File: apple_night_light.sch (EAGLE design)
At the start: 39 parts, among them U2 INA219AIDCNR, U3 ATSHA204-TSU, Y1 16MHZ

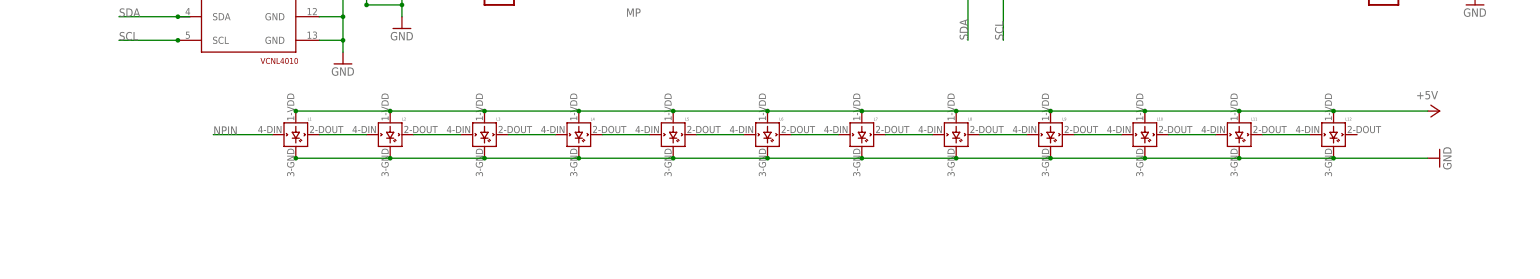
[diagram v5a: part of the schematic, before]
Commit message: converting to dotstar LEDs, still some hookup work needed
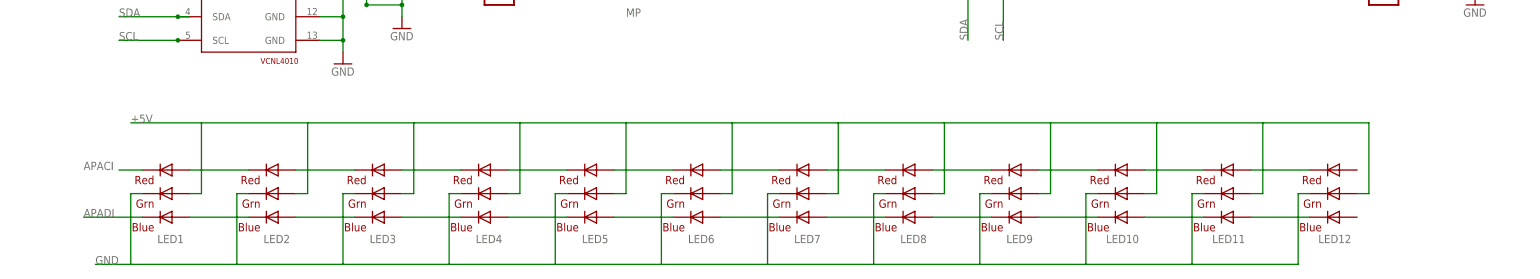
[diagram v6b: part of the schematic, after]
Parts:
- removed L1, L10, L11, L12, L2, L3, L4, L5, L6, L7, L8, L9: WS2812B, adafruit:WS2812B
- added LED1, LED10, LED11, LED12, LED2, LED3, LED4, LED5, LED6, LED7, LED8, LED9: RGBLED5050, adafruit:RGBLED5050
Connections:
- removed net N$14: L5.DOUT, L6.DIN
- removed net N$20: L7.DOUT, L8.DIN
- removed net N$28: L4.DOUT, L5.DIN
- new net APACI: LED1.RED_C
- new net APACI1: LED3.RED_A, LED4.RED_C
- new net APACI2: LED6.RED_A, LED7.RED_C
- new net APACI3: LED10.RED_C, LED9.RED_A
- new net APADI: LED1.BLUE_C
- new net N$1: LED1.RED_A, LED2.RED_C
- new net N$15: LED4.RED_A, LED5.RED_C
- new net N$18: LED4.BLUE_A, LED5.BLUE_C
- new net N$26: LED8.BLUE_A, LED9.BLUE_C
- new net N$30: LED10.RED_A, LED11.RED_C
- new net N$31: LED11.RED_A, LED12.RED_C
- new net N$32: LED10.BLUE_A, LED11.BLUE_C
- new net N$35: LED11.BLUE_A, LED12.BLUE_C
- new net N$5: LED2.BLUE_A, LED3.BLUE_C
- new net N$6: LED3.BLUE_A, LED4.BLUE_C
- new net N$8: LED6.BLUE_A, LED7.BLUE_C
- net +5V: now also LED1.GREEN_A, LED10.GREEN_A, LED11.GREEN_A, LED12.GREEN_A, LED2.GREEN_A, LED3.GREEN_A, LED4.GREEN_A, LED5.GREEN_A, LED6.GREEN_A, LED7.GREEN_A, LED8.GREEN_A, LED9.GREEN_A; no longer L1.VDD, L10.VDD, L11.VDD, L12.VDD, L2.VDD, L3.VDD, L4.VDD, L5.VDD, L6.VDD, L7.VDD, L8.VDD, L9.VDD
- net GND: now also LED1.GREEN_C, LED10.GREEN_C, LED11.GREEN_C, LED12.GREEN_C, LED2.GREEN_C, LED3.GREEN_C, LED4.GREEN_C, LED5.GREEN_C, LED6.GREEN_C, LED7.GREEN_C, LED8.GREEN_C, LED9.GREEN_C; no longer L1.GND, L10.GND, L11.GND, L12.GND, L2.GND, L3.GND, L4.GND, L5.GND, L6.GND, L7.GND, L8.GND, L9.GND
- net N$12: now also LED10.BLUE_C, LED9.BLUE_A; no longer L6.DOUT, L7.DIN
- net N$17: now also LED5.RED_A, LED6.RED_C; no longer L10.DIN, L9.DOUT
- net N$19: now also LED5.BLUE_A, LED6.BLUE_C; no longer L8.DOUT, L9.DIN
- net N$2: now also LED2.RED_A, LED3.RED_C; no longer L2.DOUT, L3.DIN
- net N$23: now also LED7.RED_A, LED8.RED_C; no longer L3.DOUT, L4.DIN
- net N$24: now also LED8.RED_A, LED9.RED_C; no longer L11.DOUT, L12.DIN
- net N$25: now also LED7.BLUE_A, LED8.BLUE_C; no longer L10.DOUT, L11.DIN
- net N$3: now also LED1.BLUE_A, LED2.BLUE_C; no longer L1.DOUT, L2.DIN
- net NPIN: no longer L1.DIN

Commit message: re-laying out the board and separating panels to an extent
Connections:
- removed net APACI: LED1.RED_C
- removed net APADI: LED1.BLUE_C
- net MOSI: now also LED1.BLUE_C
- net SCK: now also LED1.RED_C
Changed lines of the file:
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@@
 <label x="121.92" y="63.5" size="1.778" layer="95" xref="yes"/>
+</segment>
+<segment>
+<pinref part="LED1" gate="G$1" pin="BLUE_C"/>
+<wire x1="-119.38" y1="-25.4" x2="-132.08" y2="-25.4" width="0.1524" layer="91"/>
+<label x="-132.08" y="-25.4" size="1.778" layer="95"/>
 </segment>
 </net>
@@
 <wire x1="96.52" y1="63.5" x2="88.9" y2="63.5" width="0.1524" layer="91"/>
 <label x="88.9" y="63.5" size="1.778" layer="95" rot="MR0" xref="yes"/>
+</segment>
+<segment>
+<pinref part="LED1" gate="G$1" pin="RED_C"/>
+<wire x1="-119.38" y1="-15.24" x2="-124.46" y2="-15.24" width="0.1524" layer="91"/>
+<label x="-132.08" y="-15.24" size="1.778" layer="95"/>
 </segment>
 </net>
@@
 </segment>
 </net>
-<net name="APADI" class="0">
-<segment>
-<pinref part="LED1" gate="G$1" pin="BLUE_C"/>
-<wire x1="-119.38" y1="-25.4" x2="-132.08" y2="-25.4" width="0.1524" layer="91"/>
-<label x="-132.08" y="-25.4" size="1.778" layer="95"/>
-</segment>
-</net>
-<net name="APACI" class="0">
-<segment>
-<pinref part="LED1" gate="G$1" pin="RED_C"/>
-<wire x1="-119.38" y1="-15.24" x2="-124.46" y2="-15.24" width="0.1524" layer="91"/>
-<label x="-132.08" y="-15.24" size="1.778" layer="95"/>
-</segment>
-</net>

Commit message: adding balance board for space usage, tightening things up
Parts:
- added A0, A1: TPB1,27, testpad:TPB1,27
- added JP3: (no value), SparkFun-Connectors:M06NO_SILK_FEMALE_PTH
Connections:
- new net N$43: A0.TP, U2.A0
- new net N$44: A1.TP, U2.A1
- new net N$46: AOUT.1, C1.2, C2.-, C3.-, C4.2, C5.2, C7.2, DOUT.1, JP1.CTS, JP1.GND, JP2.GND, LED1.GREEN_C, LED10.GREEN_C, LED11.GREEN_C, LED12.GREEN_C, LED2.GREEN_C, LED3.GREEN_C, LED4.GREEN_C, LED5.GREEN_C, LED6.GREEN_C, LED7.GREEN_C, LED8.GREEN_C, LED9.GREEN_C, MP.AGND, MP.GND@1, MP.GND@2, NRF.1, R1.1, SPI.6, U$1.GND, U$3.GND@1, U$3.GND@2, U$3.IR-@1, U$3.IR-@2, U1.GND, U2.GND, USBOUT.GND, Y1.2
- net GND: now also JP3.1; no longer AOUT.1, C1.2, C2.-, C3.-, C4.2, C5.2, C7.2, DOUT.1, JP1.CTS, JP1.GND, JP2.GND, LED1.GREEN_C, LED10.GREEN_C, LED11.GREEN_C, LED12.GREEN_C, LED2.GREEN_C, LED3.GREEN_C, LED4.GREEN_C, LED5.GREEN_C, LED6.GREEN_C, LED7.GREEN_C, LED8.GREEN_C, LED9.GREEN_C, MP.AGND, MP.GND@1, MP.GND@2, NRF.1, R1.1, SPI.6, U$1.GND, U$3.GND@1, U$3.GND@2, U$3.IR-@1, U$3.IR-@2, U1.GND, U2.GND, USBOUT.GND, Y1.2
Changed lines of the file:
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@@
 <part name="LED12" library="adafruit" deviceset="RGBLED" device="5050"/>
 <part name="LED10" library="adafruit" deviceset="RGBLED" device="5050"/>
+<part name="A1" library="testpad" deviceset="TP" device="B1,27"/>
+<part name="A0" library="testpad" deviceset="TP" device="B1,27"/>
+<part name="JP3" library="SparkFun-Connectors" deviceset="M06" device="NO_SILK_FEMALE_PTH"/>
 </parts>
 <sheets>
@@
 <instance part="LED12" gate="G$1" x="137.16" y="-20.32" rot="R180"/>
 <instance part="LED10" gate="G$1" x="91.44" y="-20.32" rot="R180"/>
+<instance part="A1" gate="G$1" x="-119.38" y="68.58" rot="R90"/>
+<instance part="A0" gate="G$1" x="-121.92" y="78.74" rot="R90"/>
+<instance part="JP3" gate="G$1" x="104.14" y="22.86"/>
 </instances>
 <busses>
@@
 </segment>
 </net>
-<net name="GND" class="0">
+<net name="N$46" class="0">
 <segment>
 <pinref part="MP" gate="G$1" pin="AGND"/>
@@
 <wire x1="119.38" y1="60.96" x2="119.38" y2="58.42" width="0.1524" layer="91"/>
 <label x="119.38" y="58.42" size="1.778" layer="95" rot="R270" xref="yes"/>
-</segment>
-<segment>
-<pinref part="U3" gate="G$1" pin="GND"/>
-<wire x1="68.58" y1="88.9" x2="71.12" y2="88.9" width="0.1524" layer="91"/>
-<label x="71.12" y="88.9" size="1.778" layer="95" xref="yes"/>
 </segment>
 <segment>
@@
 <pinref part="U2" gate="A" pin="SCL"/>
 <wire x1="-104.14" y1="78.74" x2="-109.22" y2="78.74" width="0.1524" layer="91"/>
-<label x="-106.68" y="78.74" size="1.27" layer="95"/>
+<label x="-109.22" y="76.2" size="1.27" layer="95"/>
 </segment>
 </net>
@@
 </segment>
 </net>
+<net name="N$43" class="0">
+<segment>
+<pinref part="U2" gate="A" pin="A0"/>
+<wire x1="-104.14" y1="86.36" x2="-111.76" y2="86.36" width="0.1524" layer="91"/>
+<wire x1="-111.76" y1="86.36" x2="-111.76" y2="83.82" width="0.1524" layer="91"/>
+<wire x1="-111.76" y1="83.82" x2="-119.38" y2="83.82" width="0.1524" layer="91"/>
+<wire x1="-119.38" y1="83.82" x2="-119.38" y2="78.74" width="0.1524" layer="91"/>
+<pinref part="A0" gate="G$1" pin="TP"/>
+</segment>
+</net>
+<net name="N$44" class="0">
+<segment>
+<pinref part="U2" gate="A" pin="A1"/>
+<wire x1="-104.14" y1="83.82" x2="-109.22" y2="83.82" width="0.1524" layer="91"/>
+<wire x1="-109.22" y1="83.82" x2="-109.22" y2="81.28" width="0.1524" layer="91"/>
+<wire x1="-109.22" y1="81.28" x2="-116.84" y2="81.28" width="0.1524" layer="91"/>
+<wire x1="-116.84" y1="81.28" x2="-116.84" y2="68.58" width="0.1524" layer="91"/>
+<pinref part="A1" gate="G$1" pin="TP"/>
+</segment>
+</net>
+<net name="GND" class="0">
+<segment>
+<pinref part="U3" gate="G$1" pin="GND"/>
+<wire x1="68.58" y1="88.9" x2="71.12" y2="88.9" width="0.1524" layer="91"/>
+<label x="71.12" y="88.9" size="1.778" layer="95" xref="yes"/>
+</segment>
+<segment>
+<pinref part="JP3" gate="G$1" pin="1"/>
+<wire x1="109.22" y1="17.78" x2="111.76" y2="17.78" width="0.1524" layer="91"/>
+<label x="114.3" y="17.78" size="1.778" layer="95"/>
+</segment>
+</net>
